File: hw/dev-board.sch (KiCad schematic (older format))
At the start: 64 parts, among them CON1 BARREL_JACK, P1 USB_OTG, P10 CONN_01X06, P11 CONN_01X08, P2 CONN_02X03_ICSP, P3 CONN_02X03, P4 CONN_02X03_ICSP, P5 CONN_01X08, P6 CONN_02X03, P7 CONN_02X03_ICSP, P8 CONN_02X03_ICSP, P9 CONN_01X10, Q1 FDN340P, SW1 SW_PUSH, U1 LM2940LD-5.0, U10 TS3A44159, U2 MIC5205, U3 ATMEGA16U2, U4 23K256, U5 ATTINY85-SUR, U6 TS3A44159, U7 ATMEGA328PB-MU, U8 74LVCH1T45, U9 ATTINY85-SUR, X1 CRYSTAL, X2 RESONATOR

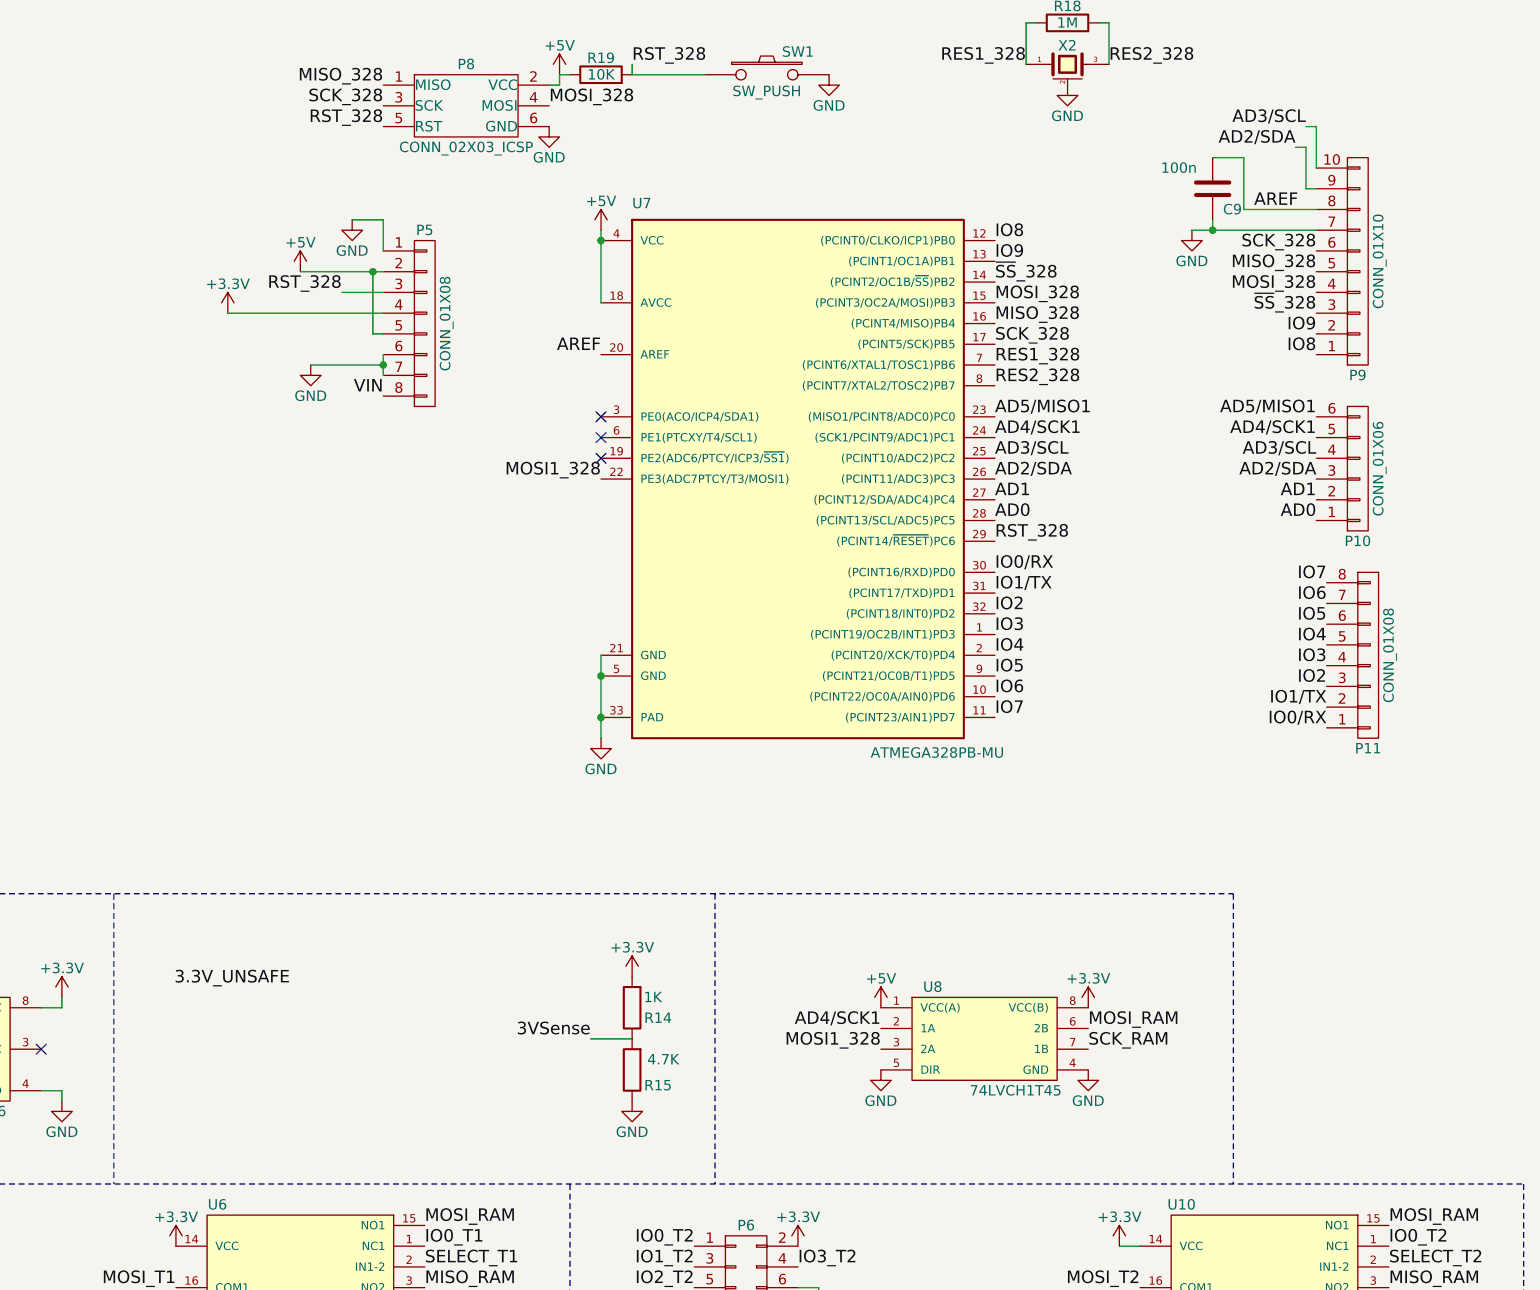
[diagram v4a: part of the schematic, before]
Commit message: Fixed added wires to IO ports and added the load switch to the drawing. I'm not 100% certain that the present configuration will work. R1 is not given a value in the DS and there is no explicit ON/OFF voltage, I'm guessing the needed voltage is related to Vds, but I don't know how yet.
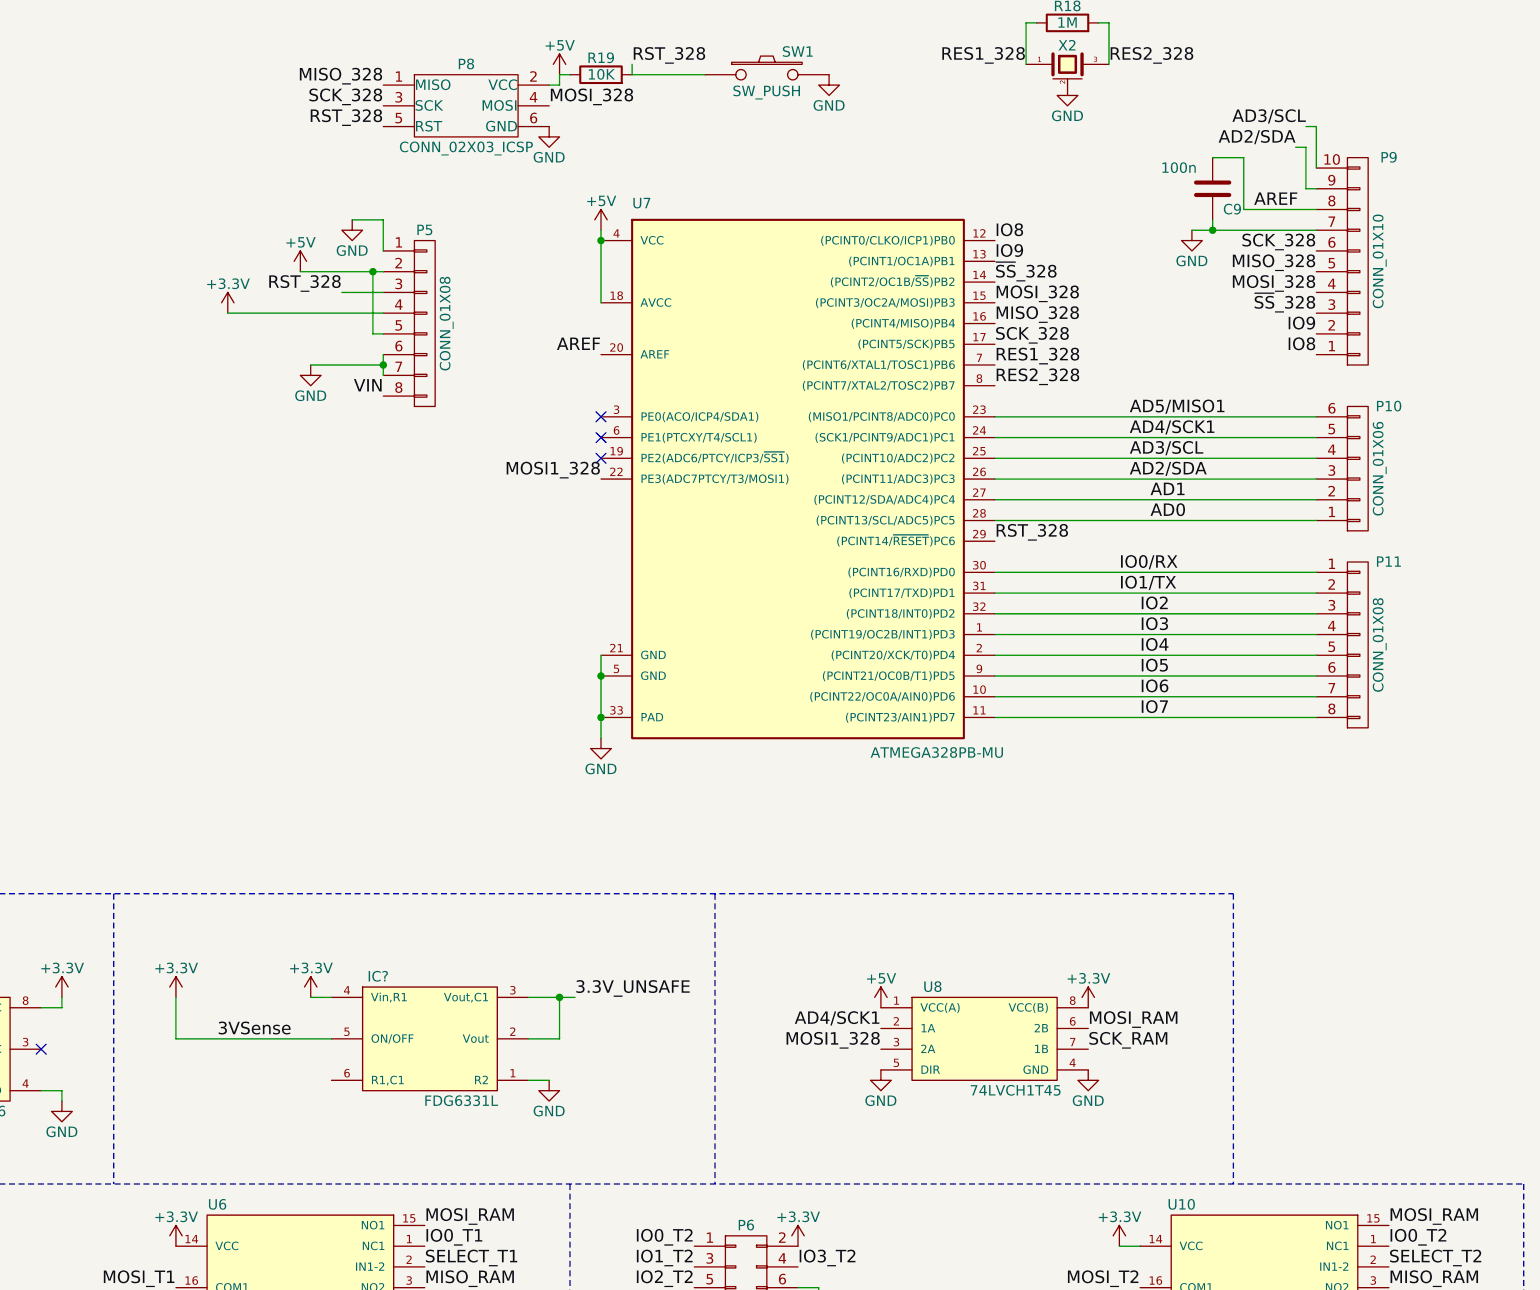
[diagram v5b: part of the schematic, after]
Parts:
- removed R14: 1K, Resistors_SMD:R_0603, symbol R
- removed R15: 4.7K, Resistors_SMD:R_0603, symbol R
- added IC?: FDG6331L, TO_SOT_Packages_SMD:SC-70-6, symbol FDG6331L
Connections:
- net +3V3: now also IC?.4 (Vin,R1), IC?.5 (ON/OFF)
- net 3.3V_UNSAFE: now also IC?.2 (Vout), IC?.3 (Vout,C1)
- net GND: now also IC?.1 (R2)
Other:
- moved on the sheet: P11
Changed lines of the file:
@@
 U 1 1 5756E20B
 P 14900 2450
-F 0 "P9" H 14900 3000 50  0000 C CNN
+F 0 "P9" H 15050 1950 50  0000 C CNN
 F 1 "CONN_01X10" V 15000 2450 50  0000 C CNN
 F 2 "Pin_Headers:Pin_Header_Straight_1x10" H 14900 2450 50  0001 C CNN
@@
 L CONN_01X08 P11
 U 1 1 5756E5AC
-P 14950 4350
-F 0 "P11" H 14950 4800 50  0000 C CNN
-F 1 "CONN_01X08" V 15050 4350 50  0000 C CNN
-F 2 "Pin_Headers:Pin_Header_Straight_1x08" H 14950 4350 50  0001 C CNN
-F 3 "" H 14950 4350 50  0000 C CNN
-	1    14950 4350
-	1    0    0    1
+P 14900 4300
+F 0 "P11" H 15050 4700 50  0000 C CNN
+F 1 "CONN_01X08" V 15000 4300 50  0000 C CNN
+F 2 "Pin_Headers:Pin_Header_Straight_1x08" H 14900 4300 50  0001 C CNN
+F 3 "" H 14900 4300 50  0000 C CNN
+	1    14900 4300
+	1    0    0    -1
 $EndComp
 $Comp
@@
 U 1 1 5756E71C
 P 14900 3450
-F 0 "P10" H 14900 3800 50  0000 C CNN
+F 0 "P10" H 15050 3150 50  0000 C CNN
 F 1 "CONN_01X06" V 15000 3450 50  0000 C CNN
 F 2 "Pin_Headers:Pin_Header_Straight_1x06" H 14900 3450 50  0001 C CNN
@@
 Text Label 13150 2550 0    60   ~ 0
 ~SS~_328
-Text Label 13150 3200 0    60   ~ 0
+Text Label 13800 3200 0    60   ~ 0
 AD5/MISO1
-Text Label 13150 3300 0    60   ~ 0
+Text Label 13800 3300 0    60   ~ 0
 AD4/SCK1
-Text Label 13150 3600 0    60   ~ 0
+Text Label 13900 3600 0    60   ~ 0
 AD1
-Text Label 13150 3700 0    60   ~ 0
+Text Label 13900 3700 0    60   ~ 0
 AD0
-Text Label 14700 3700 2    60   ~ 0
-AD0
-Text Label 14700 3600 2    60   ~ 0
-AD1
-Text Label 14700 3500 2    60   ~ 0
-AD2/SDA
-Text Label 14700 3400 2    60   ~ 0
-AD3/SCL
-Text Label 14700 3300 2    60   ~ 0
-AD4/SCK1
-Text Label 14700 3200 2    60   ~ 0
-AD5/MISO1
 Text Label 14700 2800 2    60   ~ 0
 IO9
@@
 Text Label 14700 2900 2    60   ~ 0
 IO8
-Text Label 13150 3950 0    60   ~ 0
+Text Label 13750 3950 0    60   ~ 0
 IO0/RX
-Text Label 13150 4050 0    60   ~ 0
+Text Label 13750 4050 0    60   ~ 0
 IO1/TX
-Text Label 13150 4150 0    60   ~ 0
+Text Label 13850 4150 0    60   ~ 0
 IO2
-Text Label 13150 4250 0    60   ~ 0
+Text Label 13850 4250 0    60   ~ 0
 IO3
-Text Label 13150 4350 0    60   ~ 0
+Text Label 13850 4350 0    60   ~ 0
 IO4
-Text Label 13150 4450 0    60   ~ 0
+Text Label 13850 4450 0    60   ~ 0
 IO5
-Text Label 13150 4550 0    60   ~ 0
+Text Label 13850 4550 0    60   ~ 0
 IO6
-Text Label 13150 4650 0    60   ~ 0
-IO7
-Text Label 14750 4700 2    60   ~ 0
-IO0/RX
-Text Label 14750 4600 2    60   ~ 0
-IO1/TX
-Text Label 14750 4500 2    60   ~ 0
-IO2
-Text Label 14750 4400 2    60   ~ 0
-IO3
-Text Label 14750 4300 2    60   ~ 0
-IO4
-Text Label 14750 4200 2    60   ~ 0
-IO5
-Text Label 14750 4100 2    60   ~ 0
-IO6
-Text Label 14750 4000 2    60   ~ 0
+Text Label 13850 4650 0    60   ~ 0
 IO7
 $Comp
@@
 MISO_RAM
 $Comp
-L R R14
-U 1 1 575D5900
-P 11400 6050
-F 0 "R14" H 11275 6100 50  0000 C CNN
-F 1 "1K" H 11300 6000 50  0000 C CNN
-F 2 "Resistors_SMD:R_0603" V 11330 6050 50  0001 C CNN
-F 3 "" H 11400 6050 50  0000 C CNN
-	1    11400 6050
-	-1   0    0    1
-$EndComp
-$Comp
 L GND #PWR033
 U 1 1 575D6A04
-P 11400 6500
-F 0 "#PWR033" H 11400 6250 50  0001 C CNN
-F 1 "GND" H 11400 6350 50  0000 C CNN
-F 2 "" H 11400 6500 50  0000 C CNN
-F 3 "" H 11400 6500 50  0000 C CNN
-	1    11400 6500
-	1    0    0    -1
-$EndComp
-$Comp
-L R R15
-U 1 1 575D6ADA
-P 11400 6350
-F 0 "R15" H 11275 6425 50  0000 C CNN
-F 1 "4.7K" H 11250 6300 50  0000 C CNN
-F 2 "Resistors_SMD:R_0603" V 11330 6350 50  0001 C CNN
-F 3 "" H 11400 6350 50  0000 C CNN
-	1    11400 6350
-	-1   0    0    1
+P 11000 6400
+F 0 "#PWR033" H 11000 6150 50  0001 C CNN
+F 1 "GND" H 11000 6250 50  0000 C CNN
+F 2 "" H 11000 6400 50  0000 C CNN
+F 3 "" H 11000 6400 50  0000 C CNN
+	1    11000 6400
+	-1   0    0    -1
 $EndComp
 $Comp
@@
 	1    0    0    -1
 $EndComp
-Text Label 11200 6200 2    60   ~ 0
-3VSense
 $Comp
 L +3.3V #PWR050
@@
 	1    0    0    -1
 $EndComp
-Text Label 13150 3400 0    60   ~ 0
+Text Label 13800 3400 0    60   ~ 0
 AD3/SCL
-Text Label 13150 3500 0    60   ~ 0
+Text Label 13800 3500 0    60   ~ 0
 AD2/SDA
 Text Label 14650 1800 2    60   ~ 0
@@
 	1    0    0    -1
 $EndComp
-Text Label 9750 5950 2    60   ~ 0
+Text Label 11125 6000 0    60   ~ 0
 3.3V_UNSAFE
+$Comp
+L FDG6331L IC?
+U 1 1 575EDE26
+P 10425 6200
+F 0 "IC?" H 10175 6500 50  0000 C CNN
+F 1 "FDG6331L" H 10575 5900 50  0000 C CNN
+F 2 "TO_SOT_Packages_SMD:SC-70-6" H 10625 6575 50  0001 C CIN
+F 3 "" H 10150 6150 50  0000 C CNN
+	1    10425 6200
+	1    0    0    -1
+$EndComp
 Wire Wire Line
 	2000 3100 2100 3100
@@
 	6450 9500 6450 5500
 Wire Wire Line
-	11200 6200 11400 6200
+	9200 6200 9950 6200
 Wire Notes Line
 	6450 5500 14300 5500
@@
 Wire Notes Line
 	2650 10250 1900 10250
+Wire Wire Line
+	10900 6000 11125 6000
+Wire Wire Line
+	10900 6200 11050 6200
+Wire Wire Line
+	11050 6200 11050 6000
+Connection ~ 11050 6000
 $Comp
 L +3.3V #PWR?
-U 1 1 575F0E8A
-P 11400 5900
-F 0 "#PWR?" H 11400 5750 50  0001 C CNN
-F 1 "+3.3V" H 11400 6040 50  0000 C CNN
-F 2 "" H 11400 5900 50  0000 C CNN
-F 3 "" H 11400 5900 50  0000 C CNN
-	1    11400 5900
-	1    0    0    -1
-$EndComp
+U 1 1 575EF96B
+P 9850 6000
+F 0 "#PWR?" H 9850 5850 50  0001 C CNN
+F 1 "+3.3V" H 9850 6140 50  0000 C CNN
+F 2 "" H 9850 6000 50  0000 C CNN
+F 3 "" H 9850 6000 50  0000 C CNN
+	1    9850 6000
+	-1   0    0    -1
+$EndComp
+Wire Wire Line
+	9850 6000 9950 6000
+Text Label 9400 6200 0    60   ~ 0
+3VSense
+Wire Wire Line
+	10900 6400 11000 6400
+$Comp
+L +3.3V #PWR?
+U 1 1 575F0E53
+P 9200 6000
+F 0 "#PWR?" H 9200 5850 50  0001 C CNN
+F 1 "+3.3V" H 9200 6140 50  0000 C CNN
+F 2 "" H 9200 6000 50  0000 C CNN
+F 3 "" H 9200 6000 50  0000 C CNN
+	1    9200 6000
+	-1   0    0    -1
+$EndComp
+Wire Wire Line
+	9200 6000 9200 6200
+Wire Wire Line
+	13150 4650 14700 4650
+Wire Wire Line
+	14700 4550 13150 4550
+Wire Wire Line
+	13150 4450 14700 4450
+Wire Wire Line
+	13150 4350 14700 4350
+Wire Wire Line
+	13150 4250 14700 4250
+Wire Wire Line
+	14700 4150 13150 4150
+Wire Wire Line
+	13150 4050 14700 4050
+Wire Wire Line
+	14700 3950 13150 3950
+Wire Wire Line
+	13150 3200 14700 3200
+Wire Wire Line
+	14700 3300 13150 3300
+Wire Wire Line
+	13150 3400 14700 3400
+Wire Wire Line
+	14700 3500 13150 3500
+Wire Wire Line
+	14700 3700 13150 3700
+Wire Wire Line
+	14700 3600 13150 3600
 $EndSCHEMATC

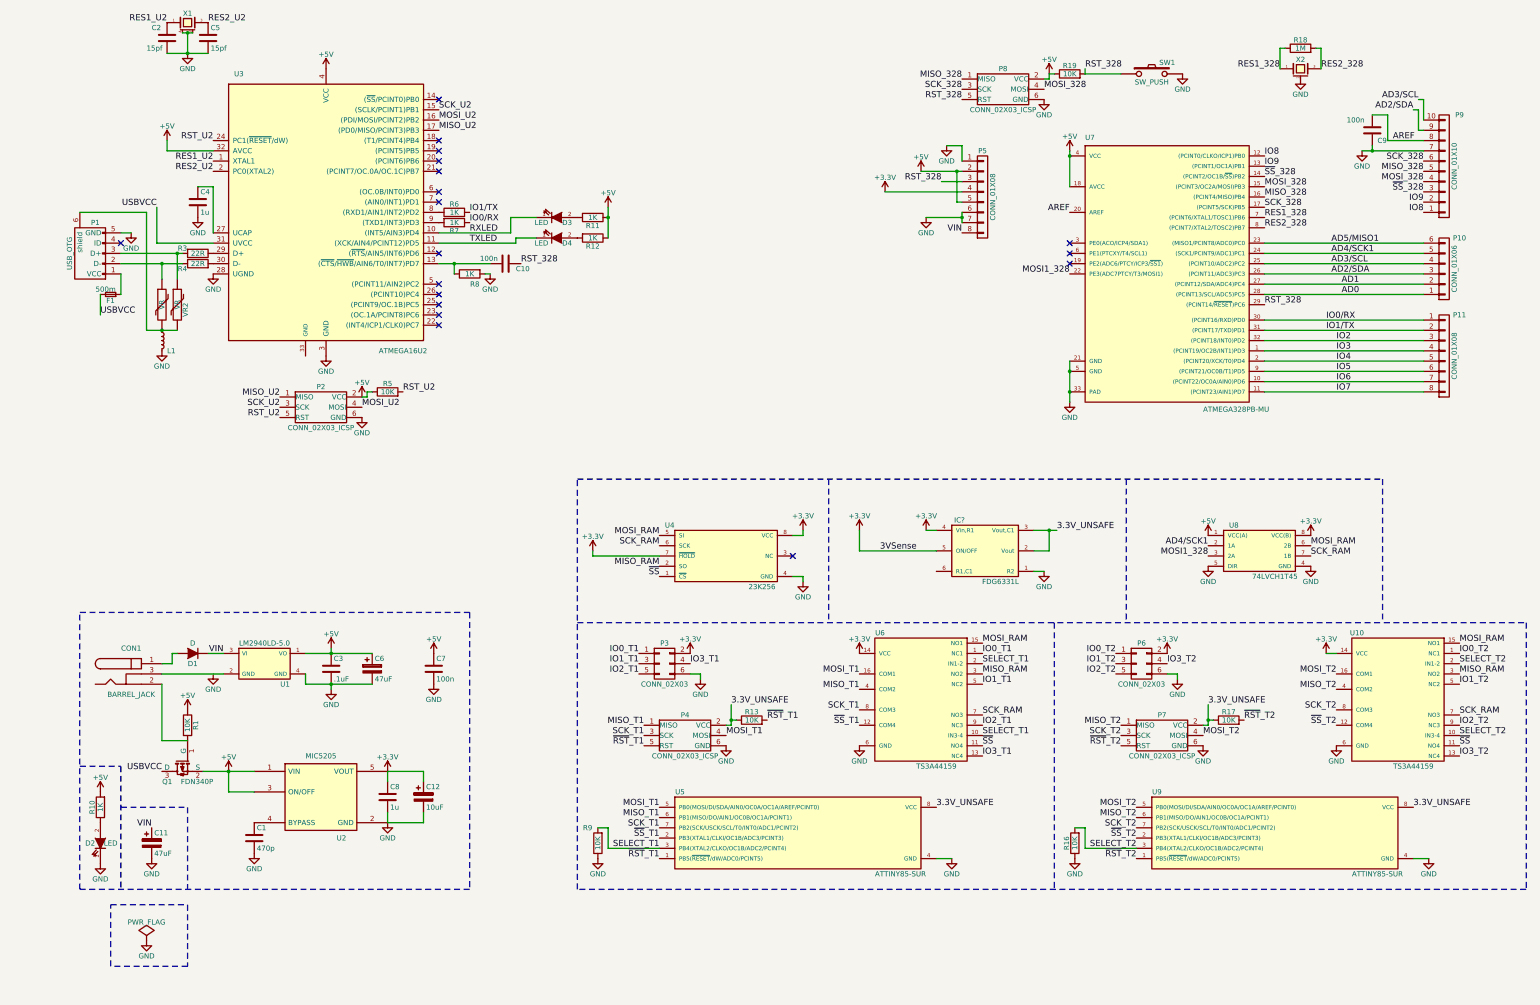
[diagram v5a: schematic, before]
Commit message: Label blocked off circuits and section off more areas in schemaic
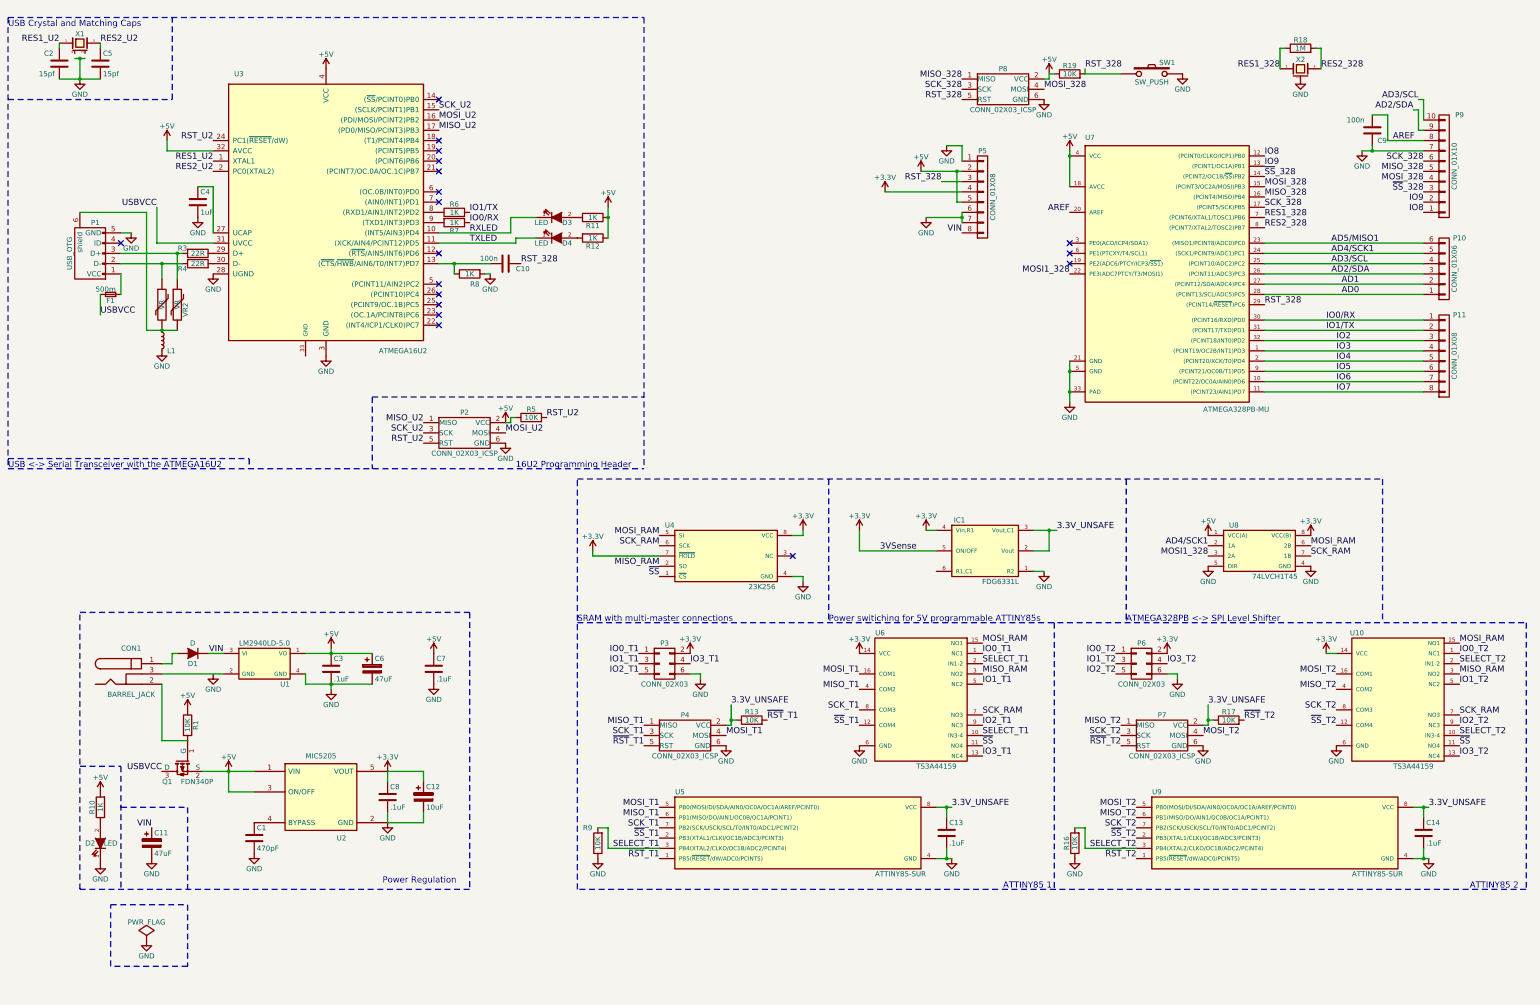
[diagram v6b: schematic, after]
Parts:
- added C13, C14: .1uF, Capacitors_SMD:C_0603, symbol C
- C1: value 470p -> 470pF
- C4: value 1u -> 1uF
- C7: value 100n -> .1uF
- C8: value 1u -> .1uF
- gave numbers to parts that had none: 1
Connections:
- net 3.3V_UNSAFE: now also C13.1, C14.1
- net GND: now also C13.2, C14.2; no longer X1.2 (case), X1.4 (0.508)
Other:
- note added: "16U2 Programming Header"
- note added: "ATMEGA328PB <-> SPI Level Shifter"
- note added: "ATTINY85 1"
- note added: "ATTINY85 2"
- note added: "Power Regulation"
- note added: "Power switiching for 5V programmable ATTINY85s"
- note added: "SRAM with multi-master connections"
- note added: "USB <-> Serial Transceiver with the ATMEGA16U2\n"
- note added: "USB Crystal and Matching Caps"
- moved on the sheet: C2, C5, P2, R5, X1
